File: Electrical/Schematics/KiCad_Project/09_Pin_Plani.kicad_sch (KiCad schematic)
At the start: 0 parts

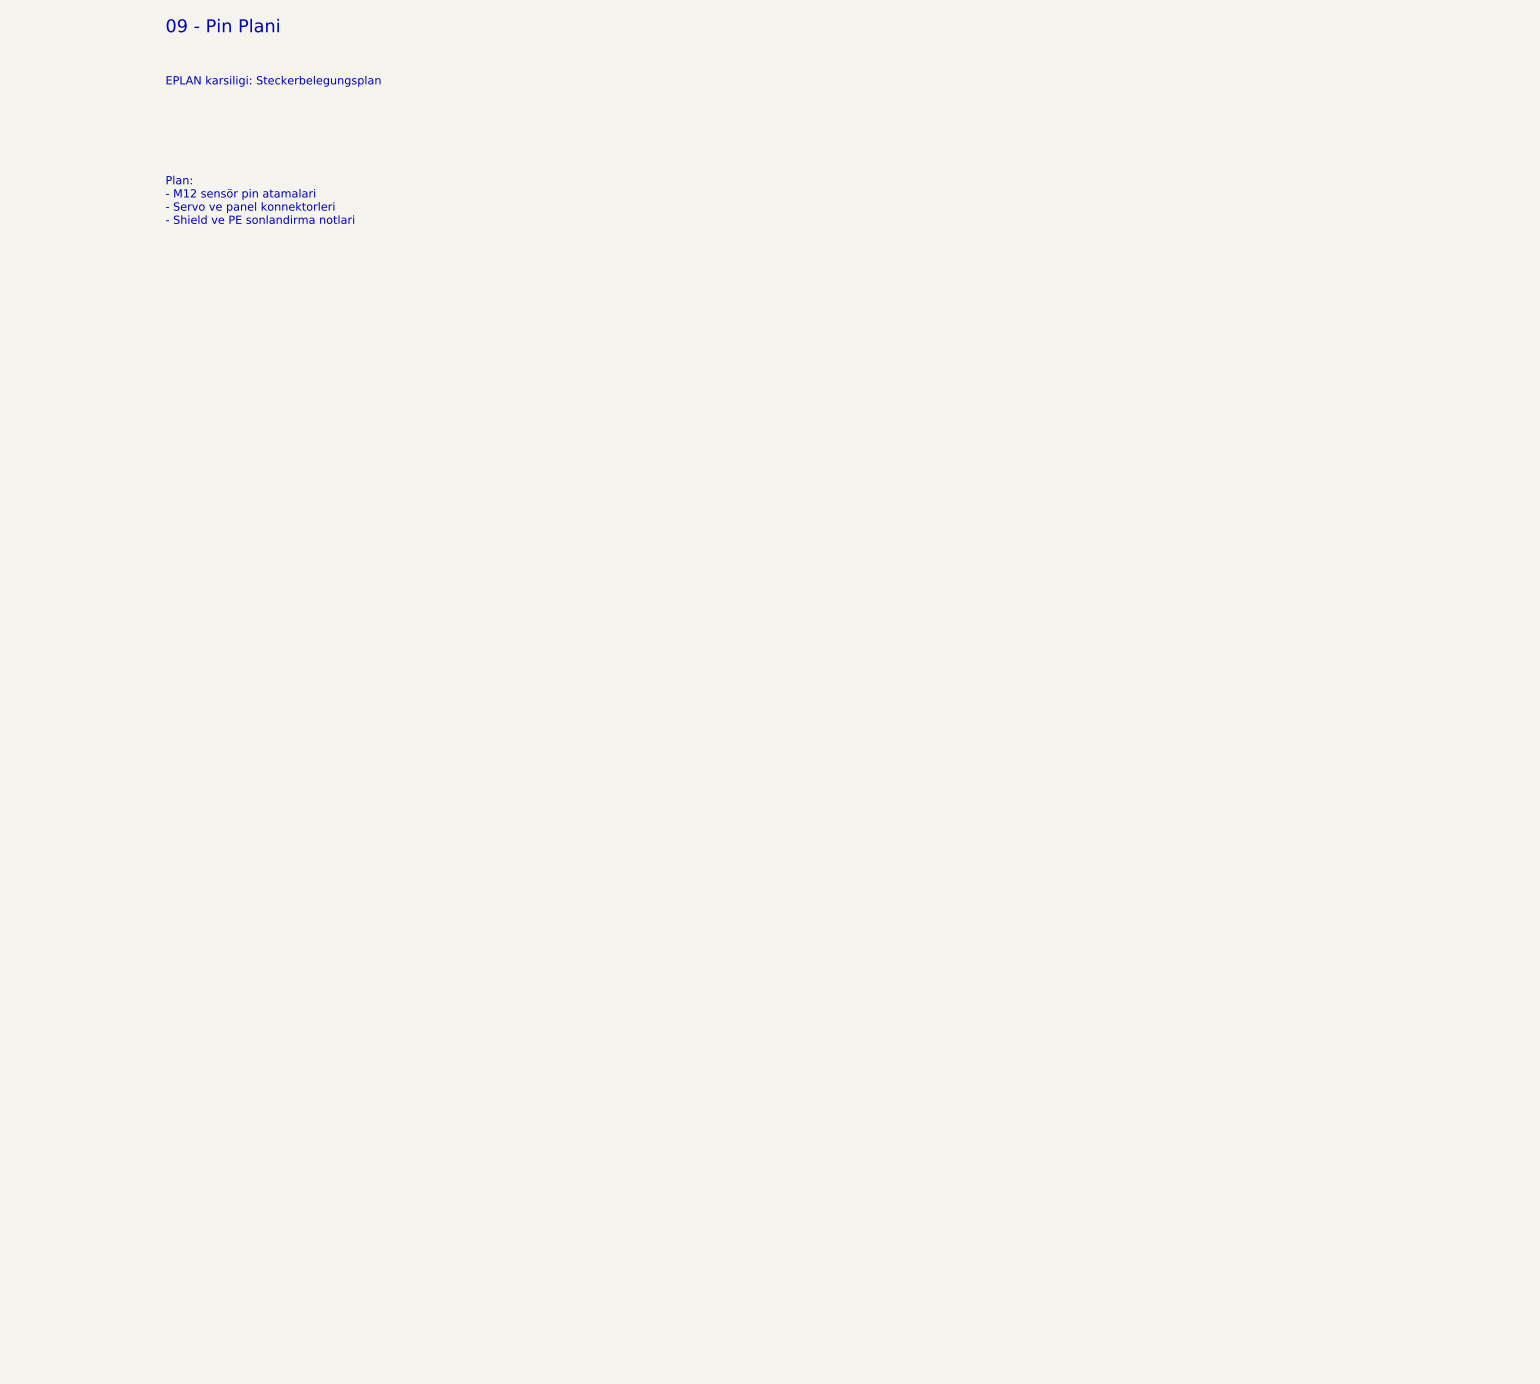
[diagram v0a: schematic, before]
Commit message: feat: update electrical schematics to rev 4.0, add technical manuals, and include project documentation and validation reports.
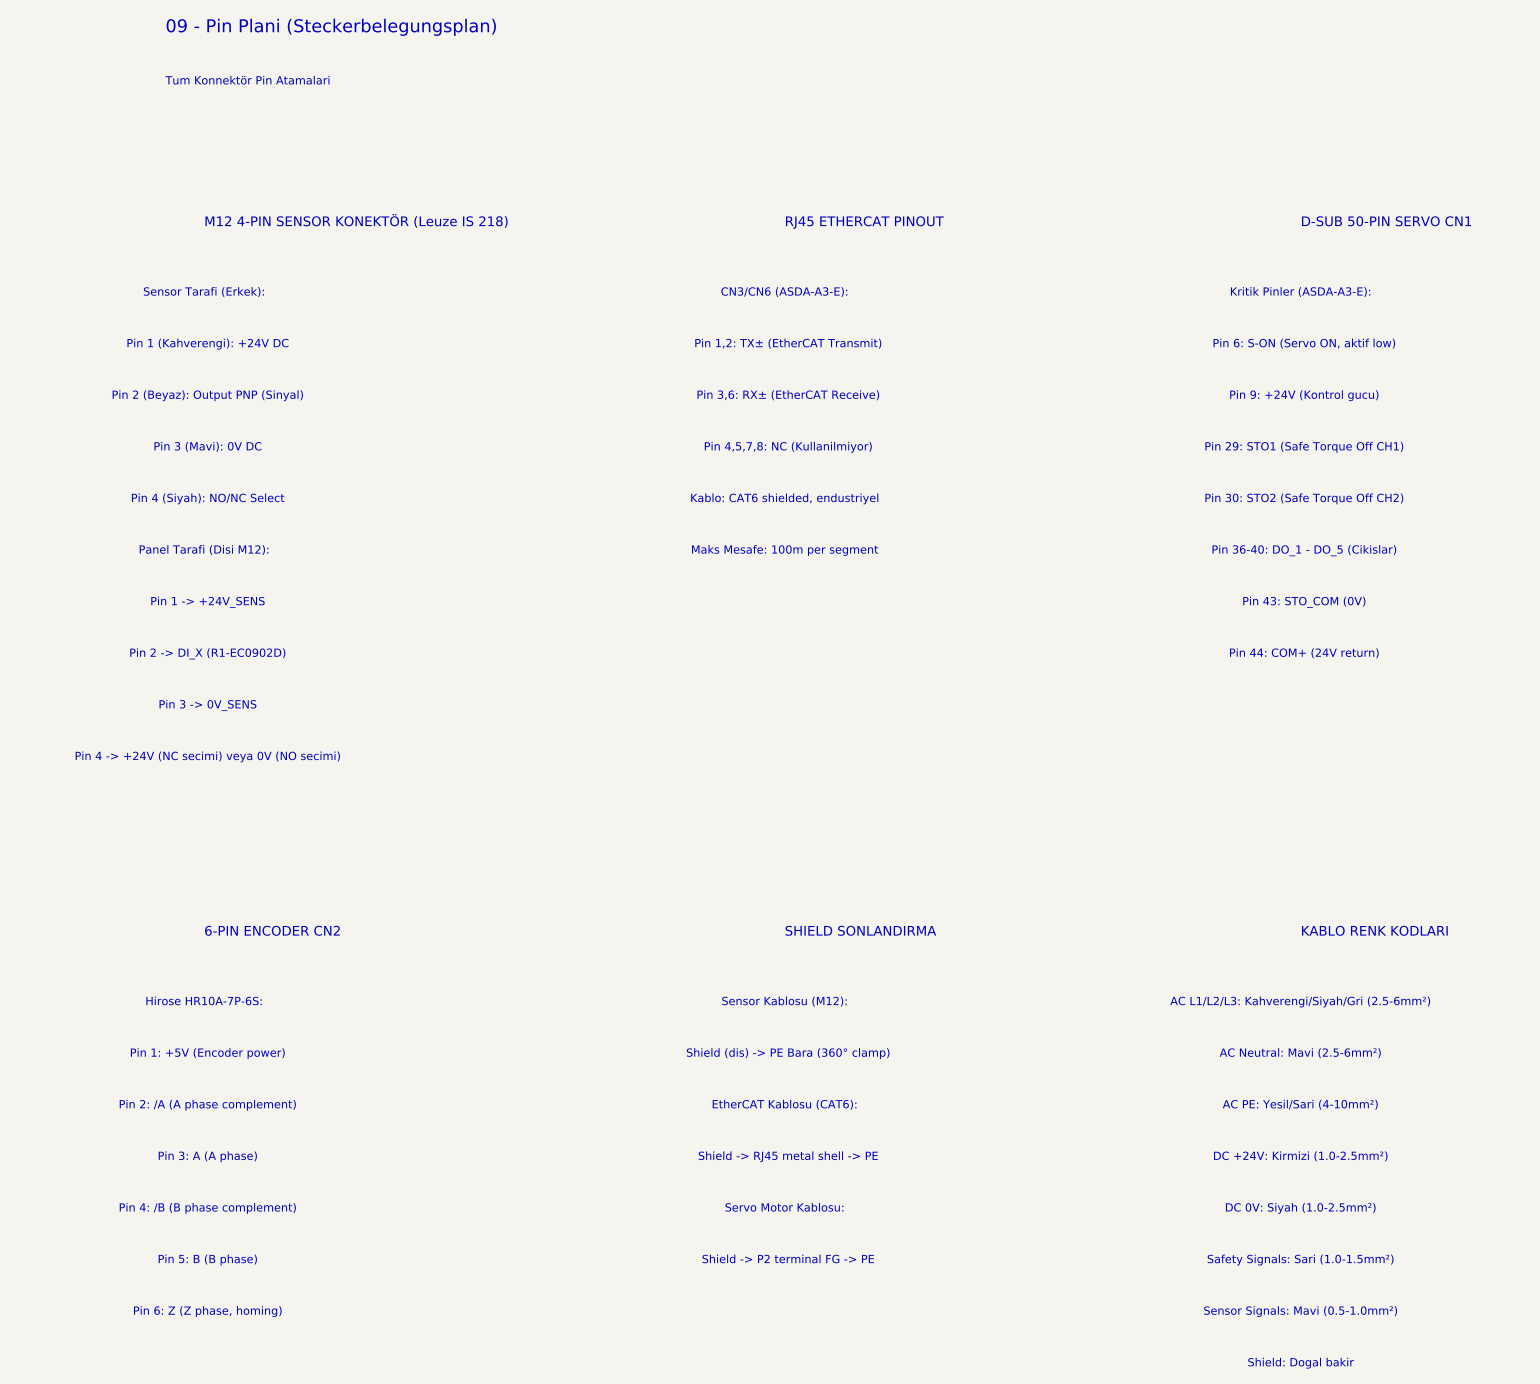
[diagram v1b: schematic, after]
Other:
- note added: "09 - Pin Plani (Steckerbelegungsplan)"
- note added: "6-PIN ENCODER CN2"
- note added: "AC L1/L2/L3: Kahverengi/Siyah/Gri (2.5-6mm²)"
- note added: "AC Neutral: Mavi (2.5-6mm²)"
- note added: "AC PE: Yesil/Sari (4-10mm²)"
- note added: "CN3/CN6 (ASDA-A3-E):"
- note added: "D-SUB 50-PIN SERVO CN1"
- note added: "DC +24V: Kirmizi (1.0-2.5mm²)"
- note added: "DC 0V: Siyah (1.0-2.5mm²)"
- note added: "EtherCAT Kablosu (CAT6):"
- note added: "Hirose HR10A-7P-6S:"
- note added: "KABLO RENK KODLARI"
- note added: "Kablo: CAT6 shielded, endustriyel"
- note added: "Kritik Pinler (ASDA-A3-E):"
- note added: "M12 4-PIN SENSOR KONEKTÖR (Leuze IS 218)"
- note added: "Maks Mesafe: 100m per segment"
- note added: "Panel Tarafi (Disi M12):"
- note added: "Pin 1 (Kahverengi): +24V DC"
- note added: "Pin 1 -> +24V_SENS"
- note added: "Pin 1,2: TX± (EtherCAT Transmit)"
- note added: "Pin 1: +5V (Encoder power)"
- note added: "Pin 2 (Beyaz): Output PNP (Sinyal)"
- note added: "Pin 2 -> DI_X (R1-EC0902D)"
- note added: "Pin 29: STO1 (Safe Torque Off CH1)"
- note added: "Pin 2: /A (A phase complement)"
- note added: "Pin 3 (Mavi): 0V DC"
- note added: "Pin 3 -> 0V_SENS"
- note added: "Pin 3,6: RX± (EtherCAT Receive)"
- note added: "Pin 30: STO2 (Safe Torque Off CH2)"
- note added: "Pin 36-40: DO_1 - DO_5 (Cikislar)"
- note added: "Pin 3: A (A phase)"
- note added: "Pin 4 (Siyah): NO/NC Select"
- note added: "Pin 4 -> +24V (NC secimi) veya 0V (NO secimi)"
- note added: "Pin 4,5,7,8: NC (Kullanilmiyor)"
- note added: "Pin 43: STO_COM (0V)"
- note added: "Pin 44: COM+ (24V return)"
- note added: "Pin 4: /B (B phase complement)"
- note added: "Pin 5: B (B phase)"
- note added: "Pin 6: S-ON (Servo ON, aktif low)"
- note added: "Pin 6: Z (Z phase, homing)"
- note added: "Pin 9: +24V (Kontrol gucu)"
- note added: "RJ45 ETHERCAT PINOUT"
- note added: "SHIELD SONLANDIRMA"
- note added: "Safety Signals: Sari (1.0-1.5mm²)"
- note added: "Sensor Kablosu (M12):"
- note added: "Sensor Signals: Mavi (0.5-1.0mm²)"
- note added: "Sensor Tarafi (Erkek):"
- note added: "Servo Motor Kablosu:"
- note added: "Shield (dis) -> PE Bara (360° clamp)"
- note added: "Shield -> P2 terminal FG -> PE"
- note added: "Shield -> RJ45 metal shell -> PE"
- note added: "Shield: Dogal bakir"
- note added: "Tum Konnektör Pin Atamalari"
- note removed: "09 - Pin Plani"
- note removed: "EPLAN karsiligi: Steckerbelegungsplan"
- note removed: "Plan: - M12 sensör pin atamalari - Servo ve panel konnektorleri - Shield ve PE sonlandirma notlari"
- company: CNCRevizyon -> CNCRevizyon - GFB60/30RE-S
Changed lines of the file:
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@@
 	(title_block
 		(title "09 Pin Plani")
-		(company "CNCRevizyon")
-		(rev "3.0")
-		(date "2026-04-05")
-	)
-	(text "09 - Pin Plani" (exclude_from_sim no) (at 24 20 0)
+		(company "CNCRevizyon - GFB60/30RE-S")
+		(rev "4.0")
+		(date "2026-04-06")
+		(comment 1 "Tum konnektör pinout'lari (M12, RJ45, D-Sub)")
+		(comment 2 "Kaynak: gfb_EP034-047170.pdf Sayfa 110-125 (Steckerbelegungsplan)")
+		(comment 3 "M12 sensor, RJ45 EtherCAT, D-Sub servo, Shield sonlandirma")
+	)
+	(text "09 - Pin Plani (Steckerbelegungsplan)" (exclude_from_sim no) (at 24 20 0)
 		(effects (font (size 2 2)) (justify left bottom))
-	)
-	(text "EPLAN karsiligi: Steckerbelegungsplan" (exclude_from_sim no) (at 24 28 0)
+		(uuid "t09001")
+	)
+	(text "Tum Konnektör Pin Atamalari" (exclude_from_sim no) (at 24 28 0)
 		(effects (font (size 1.27 1.27)) (justify left bottom))
-	)
-	(text "Plan:\n- M12 sensör pin atamalari\n- Servo ve panel konnektorleri\n- Shield ve PE sonlandirma notlari" (exclude_from_sim no) (at 24 42 0)
-		(effects (font (size 1.27 1.27)) (justify left top))
+		(uuid "t09002")
+	)
+	(text "M12 4-PIN SENSOR KONEKTÖR (Leuze IS 218)" (exclude_from_sim no) (at 30 50 0)
+		(effects (font (size 1.5 1.5)) (justify left bottom))
+		(uuid "t09010")
+	)
+	(text "Sensor Tarafi (Erkek):" (exclude_from_sim no) (at 30 60 0)
+		(effects (font (size 1.27 1.27)))
+		(uuid "t09011")
+	)
+	(text "  Pin 1 (Kahverengi): +24V DC" (exclude_from_sim no) (at 30 68 0)
+		(effects (font (size 1.27 1.27)))
+		(uuid "t09012")
+	)
+	(text "  Pin 2 (Beyaz): Output PNP (Sinyal)" (exclude_from_sim no) (at 30 76 0)
+		(effects (font (size 1.27 1.27)))
+		(uuid "t09013")
+	)
+	(text "  Pin 3 (Mavi): 0V DC" (exclude_from_sim no) (at 30 84 0)
+		(effects (font (size 1.27 1.27)))
+		(uuid "t09014")
+	)
+	(text "  Pin 4 (Siyah): NO/NC Select" (exclude_from_sim no) (at 30 92 0)
+		(effects (font (size 1.27 1.27)))
+		(uuid "t09015")
+	)
+	(text "Panel Tarafi (Disi M12):" (exclude_from_sim no) (at 30 100 0)
+		(effects (font (size 1.27 1.27)))
+		(uuid "t09016")
+	)
+	(text "  Pin 1 -> +24V_SENS" (exclude_from_sim no) (at 30 108 0)
+		(effects (font (size 1.27 1.27)))
+		(uuid "t09017")
+	)
+	(text "  Pin 2 -> DI_X (R1-EC0902D)" (exclude_from_sim no) (at 30 116 0)
+		(effects (font (size 1.27 1.27)))
+		(uuid "t09018")
+	)
+	(text "  Pin 3 -> 0V_SENS" (exclude_from_sim no) (at 30 124 0)
+		(effects (font (size 1.27 1.27)))
+		(uuid "t09019")
+	)
+	(text "  Pin 4 -> +24V (NC secimi) veya 0V (NO secimi)" (exclude_from_sim no) (at 30 132 0)
+		(effects (font (size 1.27 1.27)))
+		(uuid "t09020")
+	)
+	(text "RJ45 ETHERCAT PINOUT" (exclude_from_sim no) (at 120 50 0)
+		(effects (font (size 1.5 1.5)) (justify left bottom))
+		(uuid "t09020")
+	)
+	(text "CN3/CN6 (ASDA-A3-E):" (exclude_from_sim no) (at 120 60 0)
+		(effects (font (size 1.27 1.27)))
+		(uuid "t09021")
+	)
+	(text "  Pin 1,2: TX± (EtherCAT Transmit)" (exclude_from_sim no) (at 120 68 0)
+		(effects (font (size 1.27 1.27)))
+		(uuid "t09022")
+	)
+	(text "  Pin 3,6: RX± (EtherCAT Receive)" (exclude_from_sim no) (at 120 76 0)
+		(effects (font (size 1.27 1.27)))
+		(uuid "t09023")
+	)
+	(text "  Pin 4,5,7,8: NC (Kullanilmiyor)" (exclude_from_sim no) (at 120 84 0)
+		(effects (font (size 1.27 1.27)))
+		(uuid "t09024")
+	)
+	(text "Kablo: CAT6 shielded, endustriyel" (exclude_from_sim no) (at 120 92 0)
+		(effects (font (size 1.27 1.27)))
+		(uuid "t09025")
+	)
+	(text "Maks Mesafe: 100m per segment" (exclude_from_sim no) (at 120 100 0)
+		(effects (font (size 1.27 1.27)))
+		(uuid "t09026")
+	)
+	(text "D-SUB 50-PIN SERVO CN1" (exclude_from_sim no) (at 200 50 0)
+		(effects (font (size 1.5 1.5)) (justify left bottom))
+		(uuid "t09030")
+	)
+	(text "Kritik Pinler (ASDA-A3-E):" (exclude_from_sim no) (at 200 60 0)
+		(effects (font (size 1.27 1.27)))
+		(uuid "t09031")
+	)
+	(text "  Pin 6: S-ON (Servo ON, aktif low)" (exclude_from_sim no) (at 200 68 0)
+		(effects (font (size 1.27 1.27)))
+		(uuid "t09032")
+	)
+	(text "  Pin 9: +24V (Kontrol gucu)" (exclude_from_sim no) (at 200 76 0)
+		(effects (font (size 1.27 1.27)))
+		(uuid "t09033")
+	)
+	(text "  Pin 29: STO1 (Safe Torque Off CH1)" (exclude_from_sim no) (at 200 84 0)
+		(effects (font (size 1.27 1.27)))
+		(uuid "t09034")
+	)
+	(text "  Pin 30: STO2 (Safe Torque Off CH2)" (exclude_from_sim no) (at 200 92 0)
+		(effects (font (size 1.27 1.27)))
+		(uuid "t09035")
+	)
+	(text "  Pin 36-40: DO_1 - DO_5 (Cikislar)" (exclude_from_sim no) (at 200 100 0)
+		(effects (font (size 1.27 1.27)))
+		(uuid "t09036")
+	)
+	(text "  Pin 43: STO_COM (0V)" (exclude_from_sim no) (at 200 108 0)
+		(effects (font (size 1.27 1.27)))
+		(uuid "t09037")
+	)
+	(text "  Pin 44: COM+ (24V return)" (exclude_from_sim no) (at 200 116 0)
+		(effects (font (size 1.27 1.27)))
+		(uuid "t09038")
+	)
+	(text "6-PIN ENCODER CN2" (exclude_from_sim no) (at 30 160 0)
+		(effects (font (size 1.5 1.5)) (justify left bottom))
+		(uuid "t09040")
+	)
+	(text "Hirose HR10A-7P-6S:" (exclude_from_sim no) (at 30 170 0)
+		(effects (font (size 1.27 1.27)))
+		(uuid "t09041")
+	)
+	(text "  Pin 1: +5V (Encoder power)" (exclude_from_sim no) (at 30 178 0)
+		(effects (font (size 1.27 1.27)))
+		(uuid "t09042")
+	)
+	(text "  Pin 2: /A (A phase complement)" (exclude_from_sim no) (at 30 186 0)
+		(effects (font (size 1.27 1.27)))
+		(uuid "t09043")
+	)
+	(text "  Pin 3: A (A phase)" (exclude_from_sim no) (at 30 194 0)
+		(effects (font (size 1.27 1.27)))
+		(uuid "t09044")
+	)
+	(text "  Pin 4: /B (B phase complement)" (exclude_from_sim no) (at 30 202 0)
+		(effects (font (size 1.27 1.27)))
+		(uuid "t09045")
+	)
+	(text "  Pin 5: B (B phase)" (exclude_from_sim no) (at 30 210 0)
+		(effects (font (size 1.27 1.27)))
+		(uuid "t09046")
+	)
+	(text "  Pin 6: Z (Z phase, homing)" (exclude_from_sim no) (at 30 218 0)
+		(effects (font (size 1.27 1.27)))
+		(uuid "t09047")
+	)
+	(text "SHIELD SONLANDIRMA" (exclude_from_sim no) (at 120 160 0)
+		(effects (font (size 1.5 1.5)) (justify left bottom))
+		(uuid "t09050")
+	)
+	(text "Sensor Kablosu (M12):" (exclude_from_sim no) (at 120 170 0)
+		(effects (font (size 1.27 1.27)))
+		(uuid "t09051")
+	)
+	(text "  Shield (dis) -> PE Bara (360° clamp)" (exclude_from_sim no) (at 120 178 0)
+		(effects (font (size 1.27 1.27)))
+		(uuid "t09052")
+	)
+	(text "EtherCAT Kablosu (CAT6):" (exclude_from_sim no) (at 120 186 0)
+		(effects (font (size 1.27 1.27)))
+		(uuid "t09053")
+	)
+	(text "  Shield -> RJ45 metal shell -> PE" (exclude_from_sim no) (at 120 194 0)
+		(effects (font (size 1.27 1.27)))
+		(uuid "t09054")
+	)
+	(text "Servo Motor Kablosu:" (exclude_from_sim no) (at 120 202 0)
+		(effects (font (size 1.27 1.27)))
+		(uuid "t09055")
+	)
+	(text "  Shield -> P2 terminal FG -> PE" (exclude_from_sim no) (at 120 210 0)
+		(effects (font (size 1.27 1.27)))
+		(uuid "t09056")
+	)
+	(text "KABLO RENK KODLARI" (exclude_from_sim no) (at 200 160 0)
+		(effects (font (size 1.5 1.5)) (justify left bottom))
+		(uuid "t09060")
+	)
+	(text "AC L1/L2/L3: Kahverengi/Siyah/Gri (2.5-6mm²)" (exclude_from_sim no) (at 200 170 0)
+		(effects (font (size 1.27 1.27)))
+		(uuid "t09061")
+	)
+	(text "AC Neutral: Mavi (2.5-6mm²)" (exclude_from_sim no) (at 200 178 0)
+		(effects (font (size 1.27 1.27)))
+		(uuid "t09062")
+	)
+	(text "AC PE: Yesil/Sari (4-10mm²)" (exclude_from_sim no) (at 200 186 0)
+		(effects (font (size 1.27 1.27)))
+		(uuid "t09063")
+	)
+	(text "DC +24V: Kirmizi (1.0-2.5mm²)" (exclude_from_sim no) (at 200 194 0)
+		(effects (font (size 1.27 1.27)))
+		(uuid "t09064")
+	)
+	(text "DC 0V: Siyah (1.0-2.5mm²)" (exclude_from_sim no) (at 200 202 0)
+		(effects (font (size 1.27 1.27)))
+		(uuid "t09065")
+	)
+	(text "Safety Signals: Sari (1.0-1.5mm²)" (exclude_from_sim no) (at 200 210 0)
+		(effects (font (size 1.27 1.27)))
+		(uuid "t09066")
+	)
+	(text "Sensor Signals: Mavi (0.5-1.0mm²)" (exclude_from_sim no) (at 200 218 0)
+		(effects (font (size 1.27 1.27)))
+		(uuid "t09067")
+	)
+	(text "Shield: Dogal bakir" (exclude_from_sim no) (at 200 226 0)
+		(effects (font (size 1.27 1.27)))
+		(uuid "t09068")
 	)
 	(sheet_instances
